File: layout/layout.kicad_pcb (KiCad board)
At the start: 4 copper layers, 2 parts

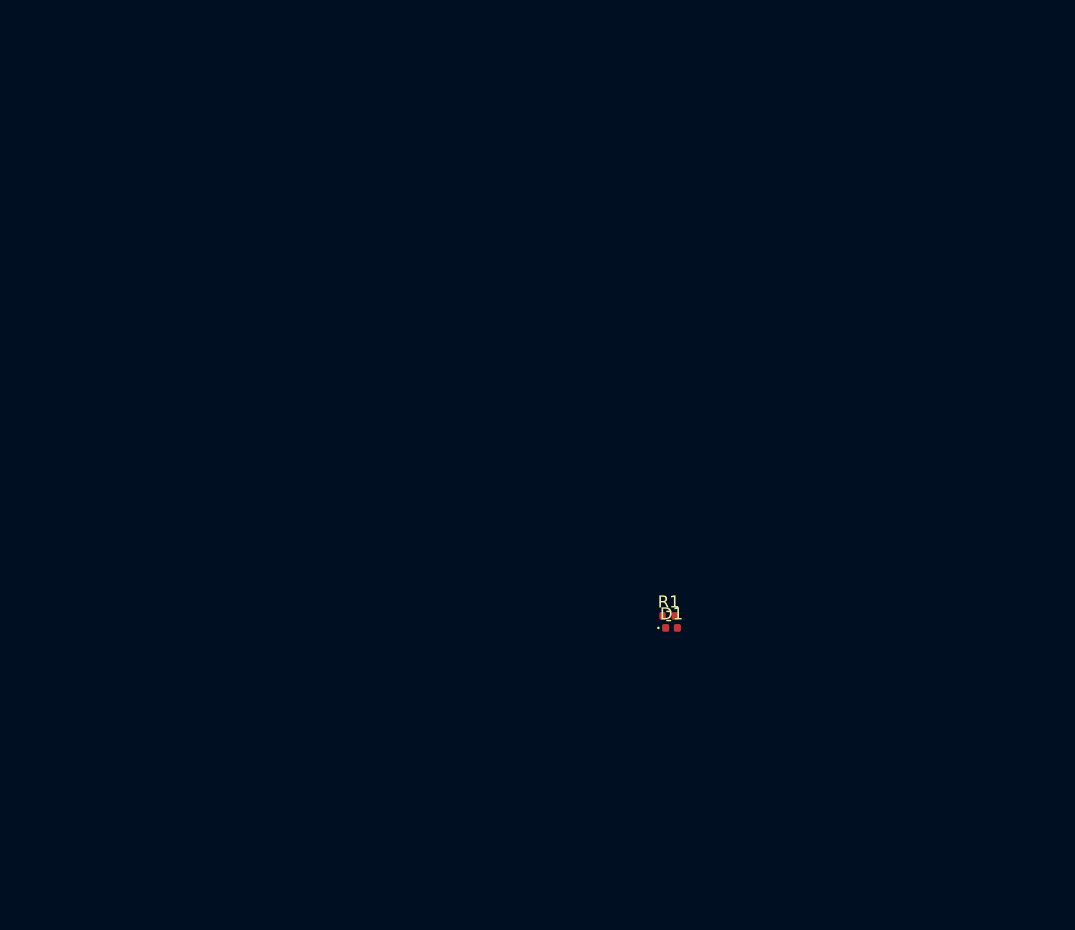
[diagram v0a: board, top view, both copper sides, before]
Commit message: Turn sample-board into a Morse transmitter
Add a CR2032 battery (BT1) and a momentary push button (SW1, the Morse key)
and wire everything in a series loop: BT1(+) -> SW1 -> R1 -> D1 -> BT1(-).
Pressing the button lights the LED (dot/dash). Adds a board outline on
Edge.Cuts; board is DRC-clean (only unrouted ratsnest remains).

Co-Authored-By: Claude Opus 4.8 (1M context) <noreply@anthropic.com>
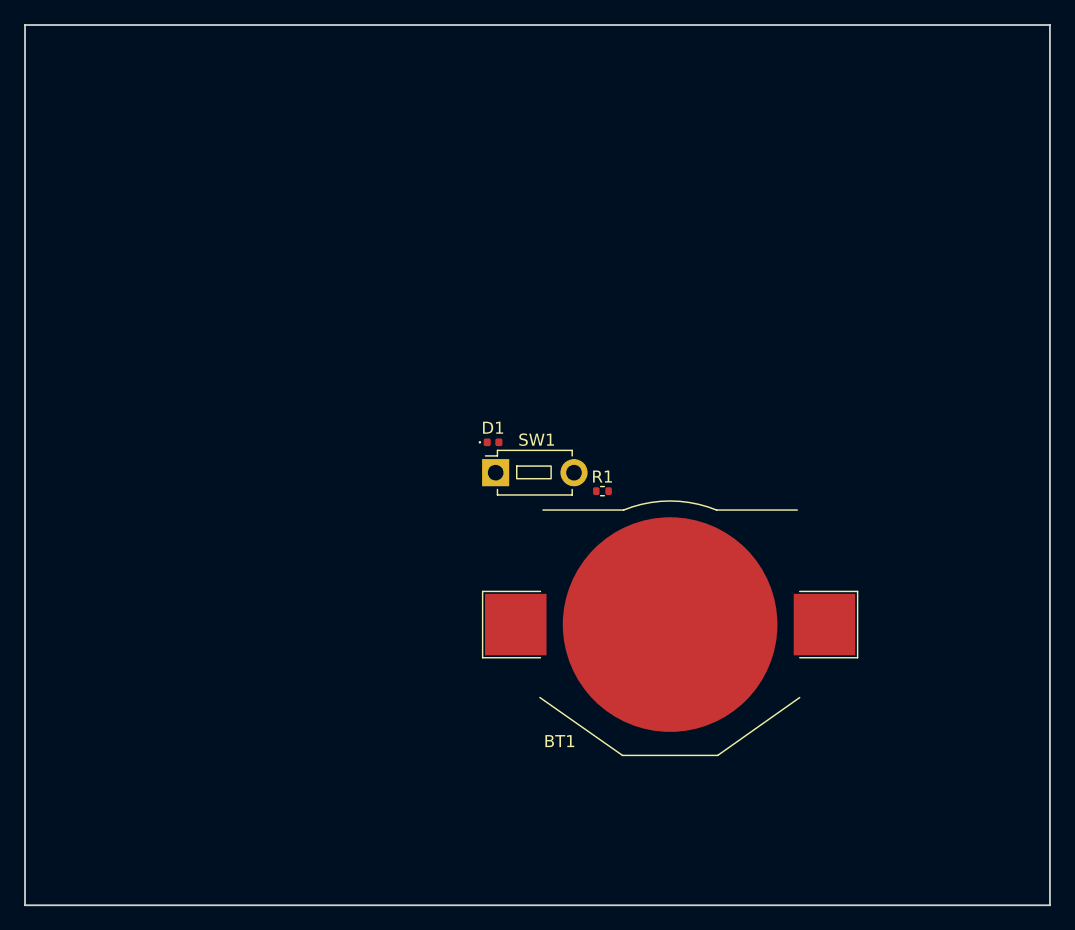
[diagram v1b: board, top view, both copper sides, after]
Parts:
- added BT1: 3002, kicad_libraries_kicad-footprints_Battery@9.0.3:BatteryHolder_Keystone_3002_1x2032, F.Cu at (148.5, 104.7)
- added SW1: MJTP1243, kicad_libraries_kicad-footprints_Button_Switch_THT@9.0.3:SW_PUSH_1P1T_6x3.5mm_H4.3_APEM_MJTP1243, F.Cu at (134.0, 92.1)
- moved D1 21.4 mm to (133.8, 89.6)
- moved R1 11.7 mm to (142.9, 93.7)
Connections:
- R1 pad 1: VCC -> KEYED
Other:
- board outline added: 85 x 73 mm
